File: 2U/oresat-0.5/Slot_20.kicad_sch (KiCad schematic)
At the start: 11 parts

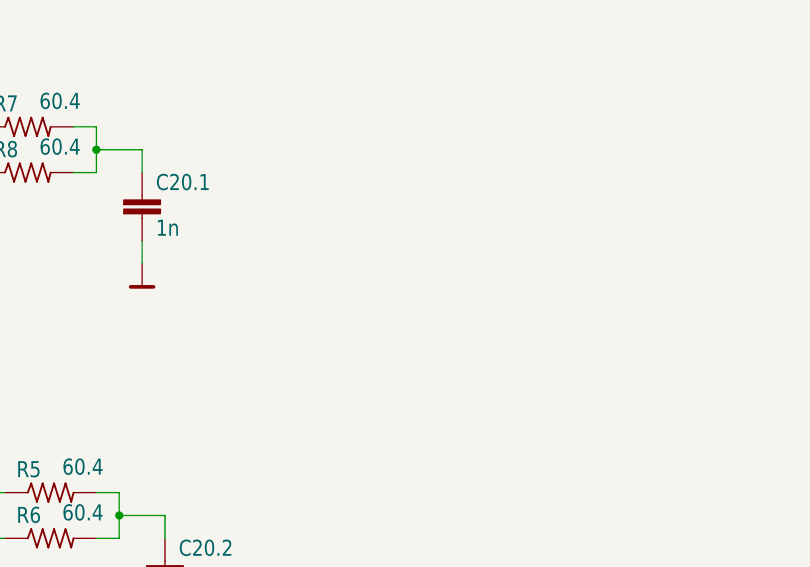
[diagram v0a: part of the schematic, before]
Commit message: Added end mounting holes and CAN connector resistors
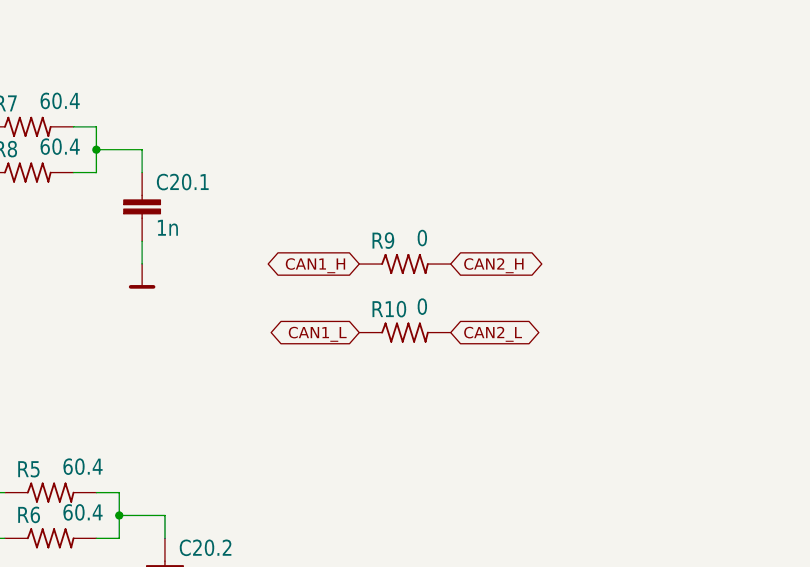
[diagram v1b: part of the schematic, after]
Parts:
- added R10, R9: 0, oresat-passives:0603-SMALL, symbol oresat-backplane-2u-eagle-import:R-US_1206-C
- R5, R6, R7, R8: footprint oresat-backplane-2u:1206-C -> Resistor_SMD:R_1206_3216Metric
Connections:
- net CAN1_H: now also R9.1
- net CAN1_L: now also R10.1
- net CAN2_H: now also R9.2
- net CAN2_L: now also R10.2
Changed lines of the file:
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@@
+    )
+  )
+  (global_label "CAN1_H" (shape bidirectional) (at 118.11 170.18 180) (fields_autoplaced)
+    (effects (font (size 1.2446 1.2446)) (justify right))
+    (property "Intersheet References" "${INTERSHEET_REFS}" (id 0) (at 166.37 363.22 0)
+      (effects (font (size 1.27 1.27)) hide)
     )
   )
@@
     (effects (font (size 1.2446 1.2446)) (justify left))
     (property "Intersheet References" "${INTERSHEET_REFS}" (id 0) (at 0 0 0)
+      (effects (font (size 1.27 1.27)) hide)
+    )
+  )
+  (global_label "CAN2_H" (shape bidirectional) (at 128.27 170.18 0) (fields_autoplaced)
+    (effects (font (size 1.2446 1.2446)) (justify left))
+    (property "Intersheet References" "${INTERSHEET_REFS}" (id 0) (at 80.01 17.78 0)
       (effects (font (size 1.27 1.27)) hide)
     )
@@
     )
   )
+  (global_label "CAN2_L" (shape bidirectional) (at 128.27 177.8 0) (fields_autoplaced)
+    (effects (font (size 1.2446 1.2446)) (justify left))
+    (property "Intersheet References" "${INTERSHEET_REFS}" (id 0) (at 80.01 20.32 0)
+      (effects (font (size 1.27 1.27)) hide)
+    )
+  )
   (global_label "CAN1_H" (shape bidirectional) (at 48.26 193.04 0) (fields_autoplaced)
     (effects (font (size 1.2446 1.2446)) (justify left))
@@
     )
   )
+  (global_label "CAN1_L" (shape bidirectional) (at 118.11 177.8 180) (fields_autoplaced)
+    (effects (font (size 1.2446 1.2446)) (justify right))
+    (property "Intersheet References" "${INTERSHEET_REFS}" (id 0) (at 166.37 375.92 0)
+      (effects (font (size 1.27 1.27)) hide)
+    )
+  )
   (symbol (lib_id "oresat-backplane-2u-eagle-import:R-US_1206-C") (at 81.28 154.94 0) (unit 1)
     (in_bom yes) (on_board yes)
@@
       (effects (font (size 1.778 1.5113)) (justify left bottom))
     )
-    (property "Footprint" "oresat-backplane-2u:1206-C" (id 2) (at 81.28 154.94 0)
+    (property "Footprint" "Resistor_SMD:R_1206_3216Metric" (id 2) (at 81.28 154.94 0)
       (effects (font (size 1.27 1.27)) hide)
     )
@@
     )
     (property "Datasheet" "" (id 3) (at 96.52 203.2 0)
+      (effects (font (size 1.27 1.27)) hide)
+    )
+    (pin "1")
+    (pin "2")
+  )
+  (symbol (lib_id "oresat-backplane-2u-eagle-import:R-US_1206-C") (at 123.19 170.18 0) (unit 1)
+    (in_bom yes) (on_board yes)
+    (property "Reference" "R9" (id 0) (at 119.38 168.6814 0)
+      (effects (font (size 1.778 1.5113)) (justify left bottom))
+    )
+    (property "Value" "0" (id 1) (at 124.46 168.402 0)
+      (effects (font (size 1.778 1.5113)) (justify left bottom))
+    )
+    (property "Footprint" "oresat-passives:0603-SMALL" (id 2) (at 123.19 170.18 0)
+      (effects (font (size 1.27 1.27)) hide)
+    )
+    (property "Datasheet" "" (id 3) (at 123.19 170.18 0)
       (effects (font (size 1.27 1.27)) hide)
     )
@@
     (pin "1")
   )
+  (symbol (lib_id "oresat-backplane-2u-eagle-import:R-US_1206-C") (at 123.19 177.8 0) (unit 1)
+    (in_bom yes) (on_board yes)
+    (property "Reference" "R10" (id 0) (at 119.38 176.3014 0)
+      (effects (font (size 1.778 1.5113)) (justify left bottom))
+    )
+    (property "Value" "0" (id 1) (at 124.46 176.022 0)
+      (effects (font (size 1.778 1.5113)) (justify left bottom))
+    )
+    (property "Footprint" "oresat-passives:0603-SMALL" (id 2) (at 123.19 177.8 0)
+      (effects (font (size 1.27 1.27)) hide)
+    )
+    (property "Datasheet" "" (id 3) (at 123.19 177.8 0)
+      (effects (font (size 1.27 1.27)) hide)
+    )
+    (pin "1")
+    (pin "2")
+  )
   (symbol (lib_id "oresat-backplane-2u-eagle-import:GND") (at 203.2 177.8 0) (unit 1)
     (in_bom yes) (on_board yes)
@@
       (effects (font (size 1.778 1.5113)) (justify left bottom))
     )
-    (property "Footprint" "oresat-backplane-2u:1206-C" (id 2) (at 81.28 160.02 0)
+    (property "Footprint" "Resistor_SMD:R_1206_3216Metric" (id 2) (at 81.28 160.02 0)
       (effects (font (size 1.27 1.27)) hide)
     )
@@
       (effects (font (size 1.778 1.5113)) (justify left bottom))
     )
-    (property "Footprint" "oresat-backplane-2u:1206-C" (id 2) (at 83.82 200.66 0)
+    (property "Footprint" "Resistor_SMD:R_1206_3216Metric" (id 2) (at 83.82 200.66 0)
       (effects (font (size 1.27 1.27)) hide)
     )
@@
       (effects (font (size 1.778 1.5113)) (justify left bottom))
     )
-    (property "Footprint" "oresat-backplane-2u:1206-C" (id 2) (at 83.82 195.58 0)
-      (effects (font (size 1.27 1.27)) hide)
-    )
+    (property "Footprint" "Resistor_SMD:R_1206_3216Metric" (id 2) (at 83.82 195.58 0)
+      (effects (font (size 1.27 1.27)) hide)
+    )

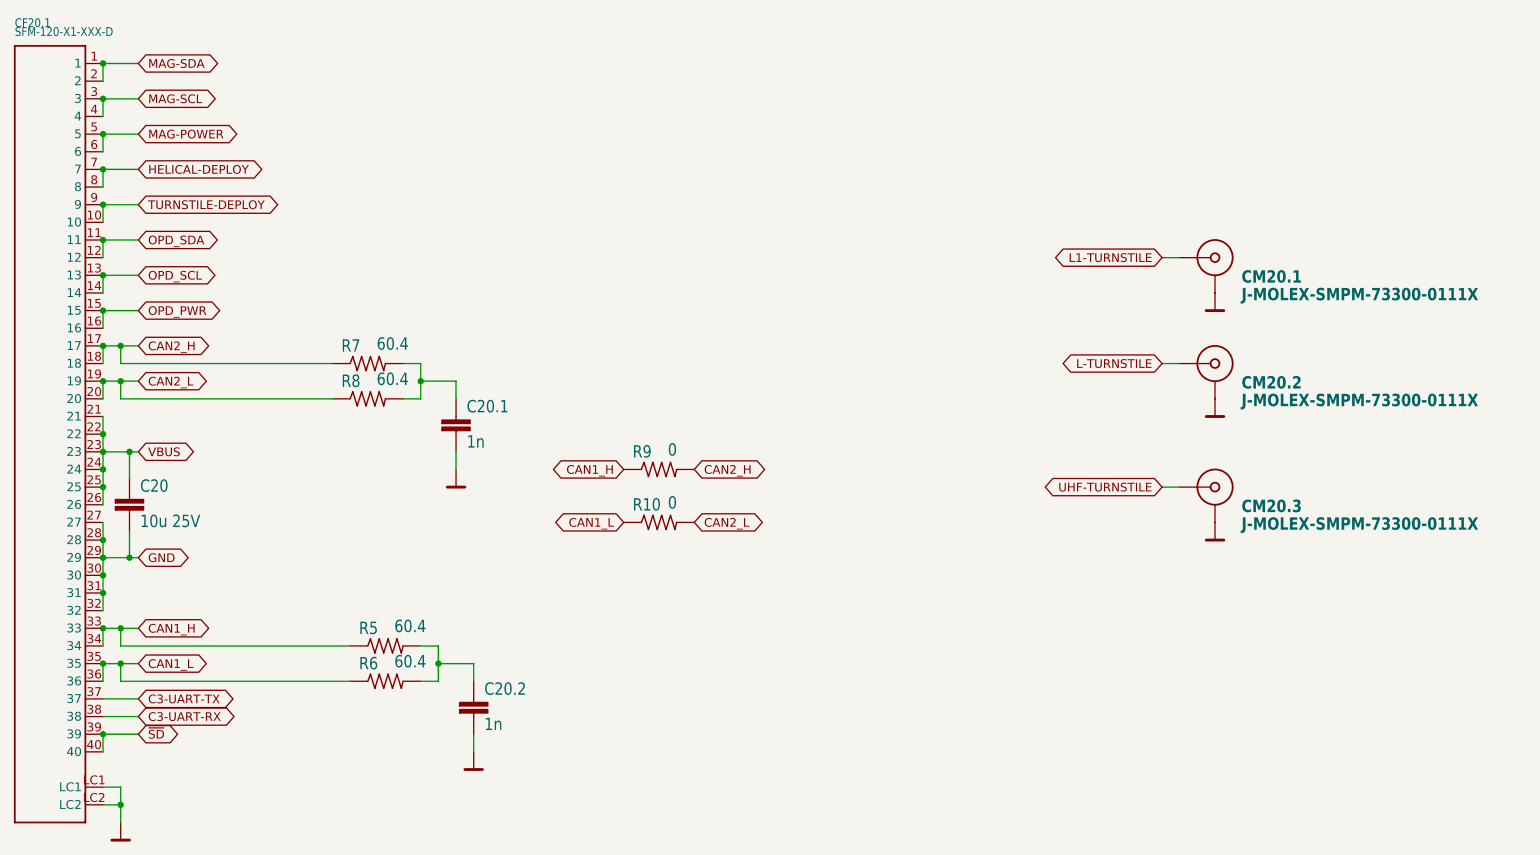
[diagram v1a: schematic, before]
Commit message: Fixed all (most) of the issues from Eagle imports
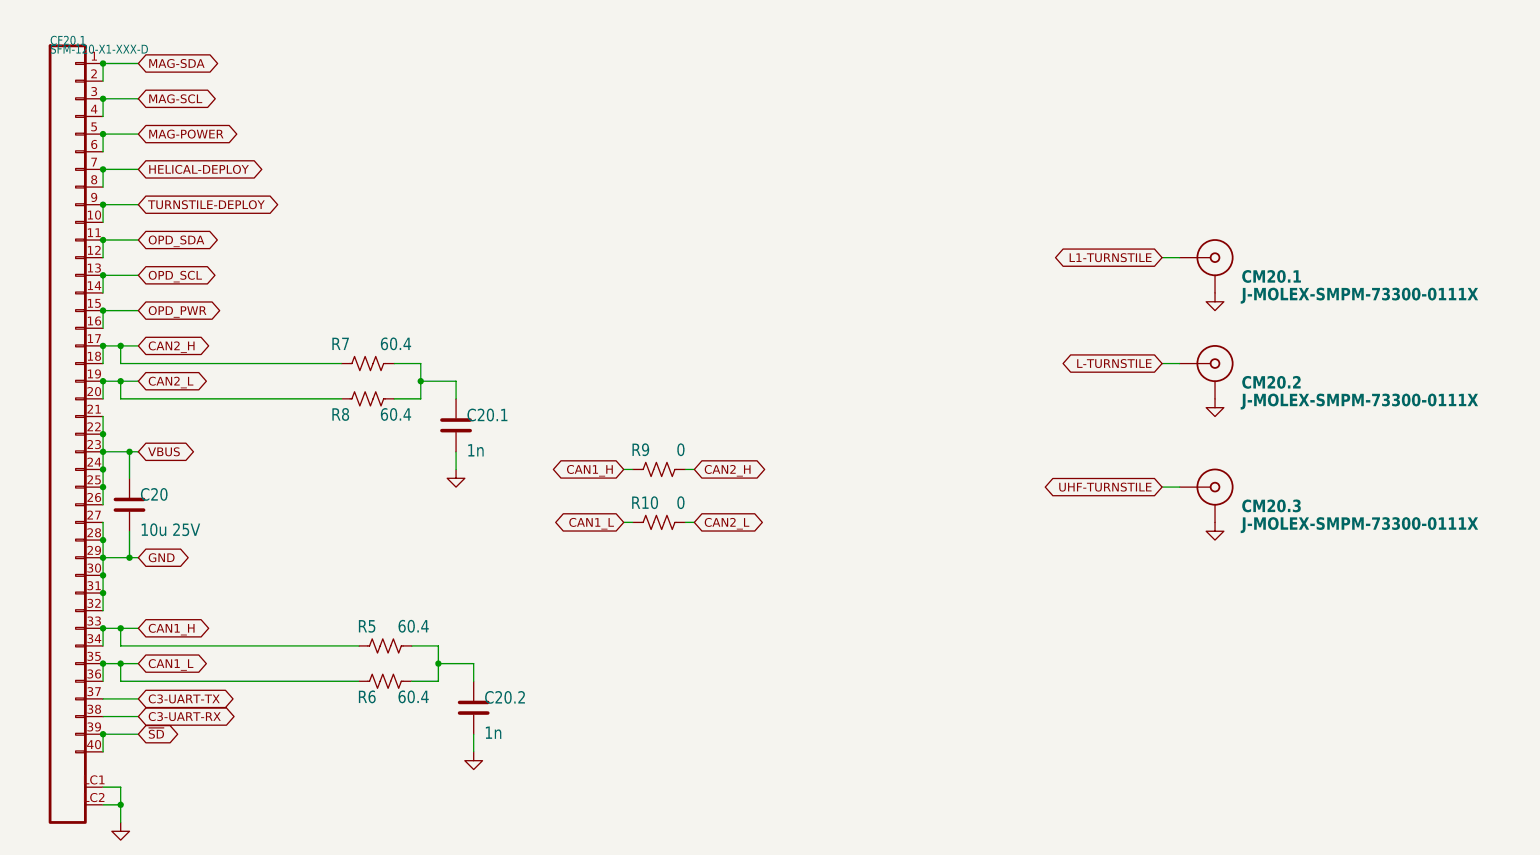
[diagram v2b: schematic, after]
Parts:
- C20: symbol oresat0-1u-backplane-eagle-import:C-EU1206-B -> Device:C
- C20.1, C20.2: symbol oresat-backplane-2u-eagle-import:C-EU0603-C-NOSILK -> Device:C
- CF20.1: symbol oresat-backplane-2u-eagle-import:SFM-120-X1-XXX-D -> oresat-connectors:J-SAMTEC-TFM-120-01-L-D-RA
- CM20.1, CM20.2, CM20.3: symbol oresat-symbols:J-MOLEX-SMPM-73300-0111X_1 -> oresat-connectors:J-MOLEX-SMPM-73300-0111X_1
- R10, R5, R6, R7, R8, R9: symbol oresat-backplane-2u-eagle-import:R-US_1206-C -> Device:R_US

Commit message: Moved entire schematic to single page
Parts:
- removed C20: 10u 25V, Capacitor_SMD:C_1206_3216Metric, symbol Device:C
- removed C20.1, C20.2: 1n, oresat-passives:0603-SMALL, symbol Device:C
- removed CF20.1: SFM-120-X1-XXX-D, oresat-connectors:J-SAMTEC-SFM-120-X1-XXX-D, symbol oresat-connectors:J-SAMTEC-TFM-120-01-L-D-RA
- removed CM20.1, CM20.2, CM20.3: J-MOLEX-SMPM-73300-0111X, oresat-connectors:J-MOLEX-SMPM-73300-0111X-long, symbol oresat-connectors:J-MOLEX-SMPM-73300-0111X_1
- removed R10, R9: 0, oresat-passives:0603-SMALL, symbol Device:R_US
- removed R5, R6, R7, R8: 60.4, Resistor_SMD:R_1206_3216Metric, symbol Device:R_US
